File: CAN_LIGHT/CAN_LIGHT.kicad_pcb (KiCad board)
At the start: 2 copper layers, 135.5 x 115.4 mm, 180 parts, among them J1 Conn_ARM_SWD_TagConnect_TC2030, J2 436500428, J3 430450428, U1 MSPM0C1103SDDFR

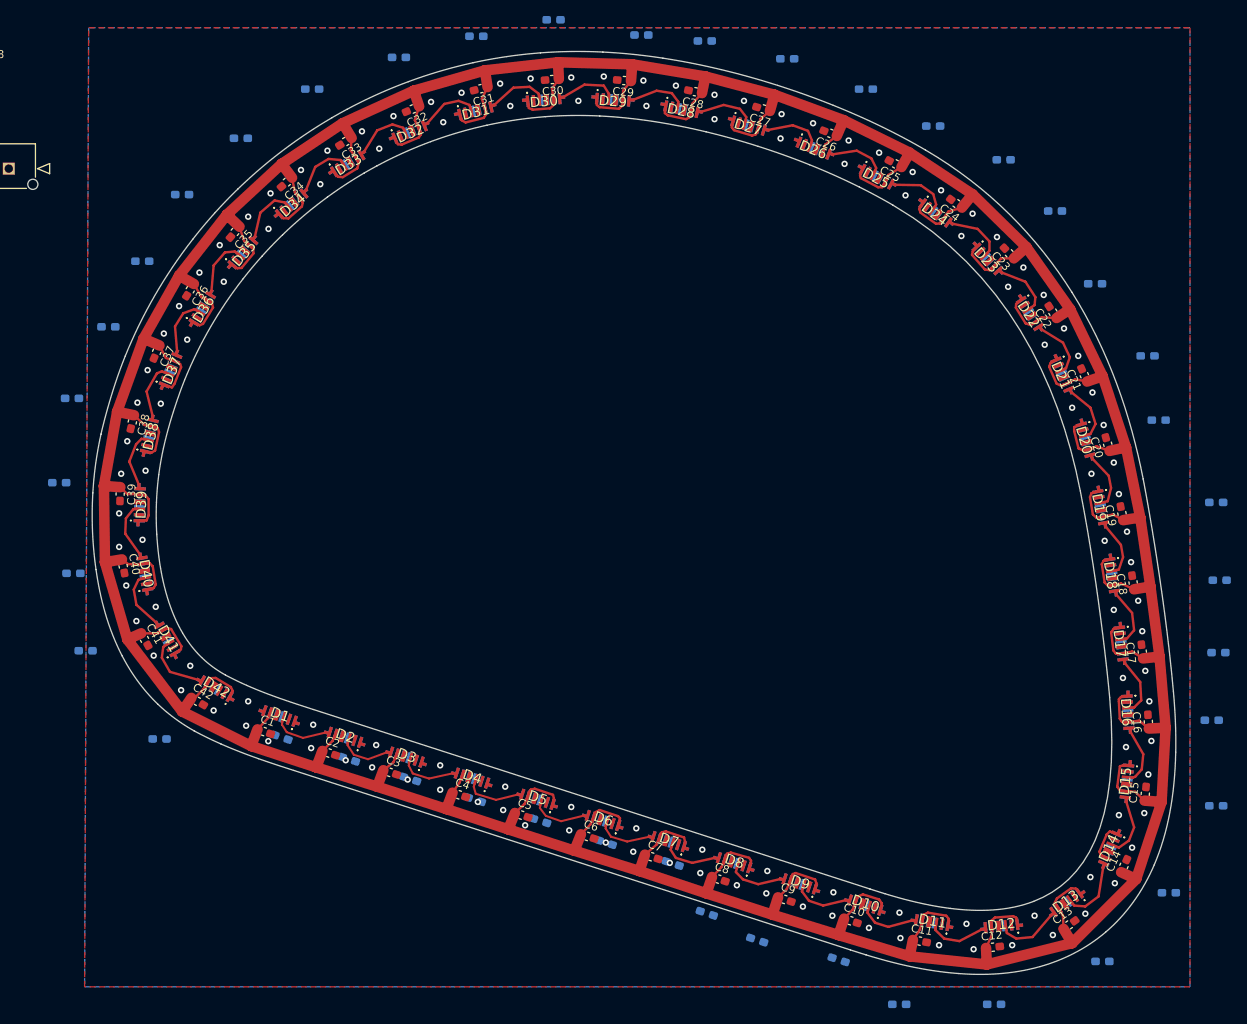
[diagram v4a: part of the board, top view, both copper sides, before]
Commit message: Roughly place caps; output updated PCB STEP file
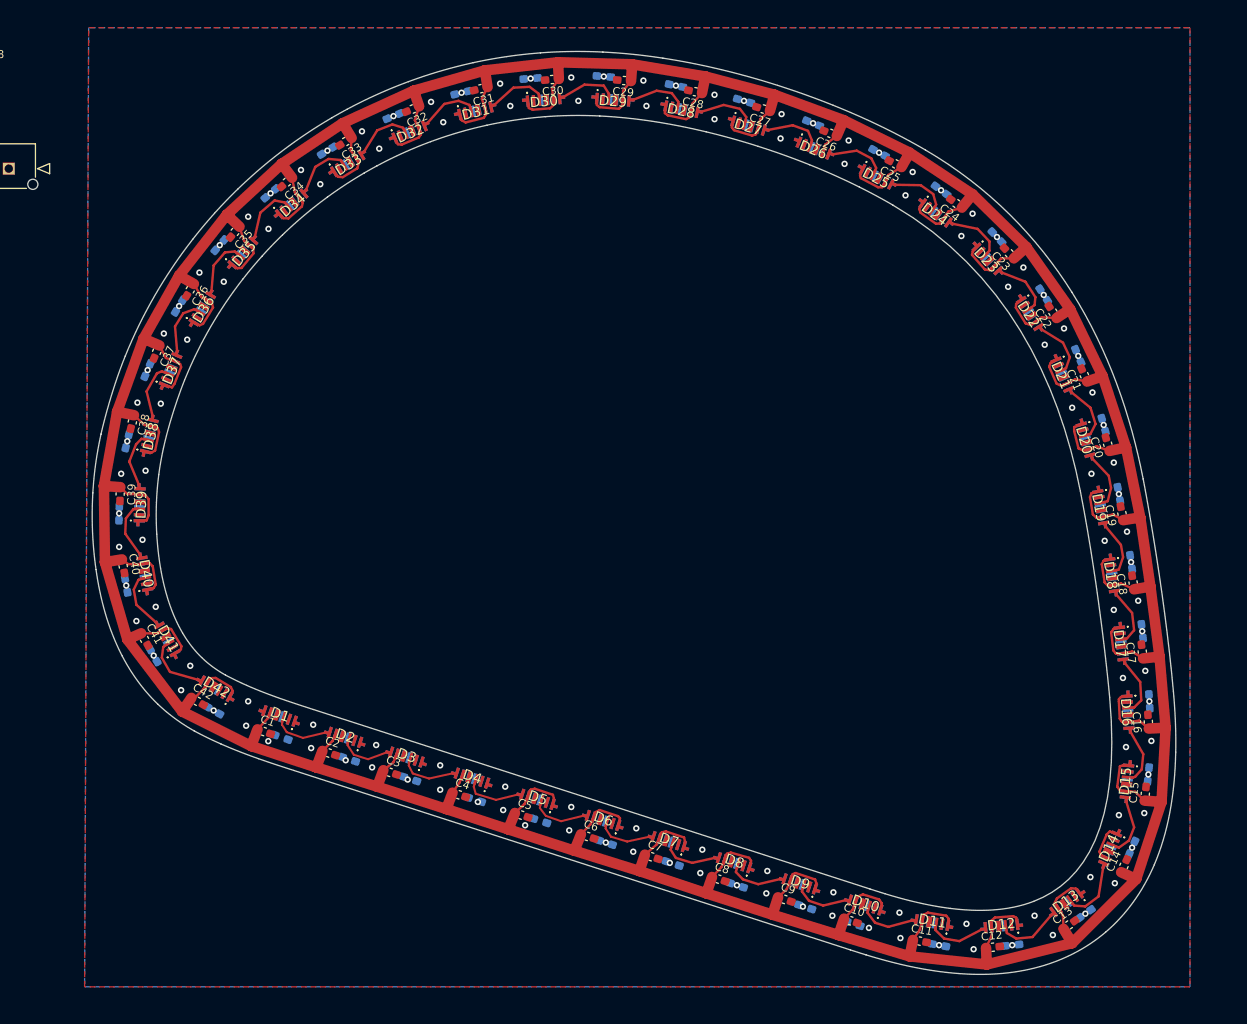
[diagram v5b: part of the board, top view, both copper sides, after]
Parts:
- moved C64 12.2 mm to (194.3, 83.1), turned to -79.5 degrees
- moved C63 11.3 mm to (195.8, 91.6), turned to -81.5 degrees
- moved C62 9.89 mm to (197.2, 100.2), turned to -83.5 degrees
- moved C60 9.34 mm to (198.0, 118.1), turned to -96 degrees
- moved C56 8.91 mm to (171.8, 139.4), turned to 170 degrees
- moved C83 8.74 mm to (70.4, 76.5), turned to 76.25 degrees
- moved C69 8.70 mm to (172.1, 45.1), turned to -36.5 degrees
- moved C66 8.66 mm to (189.2, 65.8), turned to -66.5 degrees
- moved C86 8.53 mm to (73.7, 103.3), turned to 119.25 degrees
- moved C84 8.42 mm to (69.3, 85.5), turned to 88.4 degrees
- moved C61 8.15 mm to (198.1, 109.0), turned to -86.5 degrees
- moved C68 7.96 mm to (179.1, 50.9), turned to -47 degrees
- moved C78 7.93 mm to (95.4, 40.1), turned to 31.5 degrees
- moved C75 7.88 mm to (120.8, 31.1), turned to 4.5 degrees
- moved C80 7.88 mm to (81.9, 51.9), turned to 49.25 degrees
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
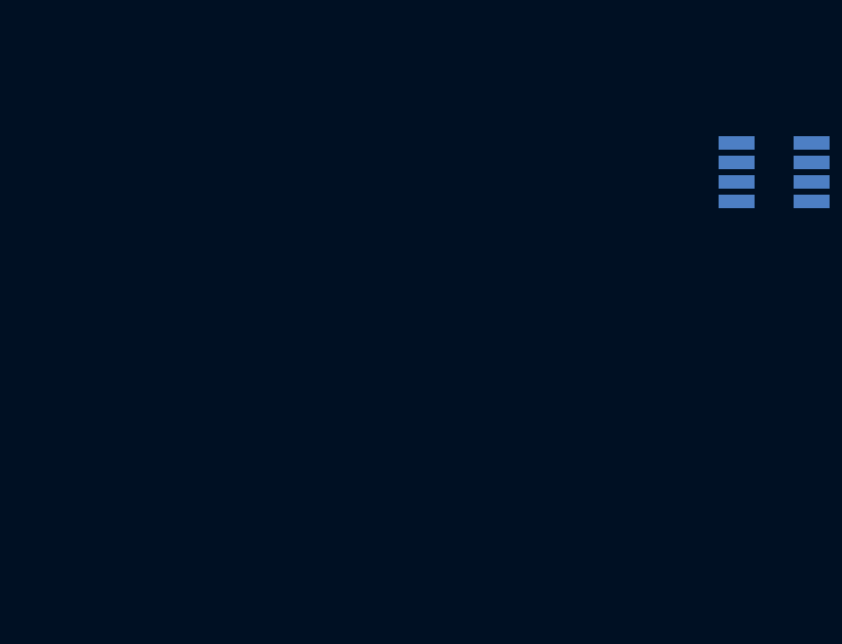
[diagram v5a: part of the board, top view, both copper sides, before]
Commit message: Select new MCU with CAN controller peripheral included
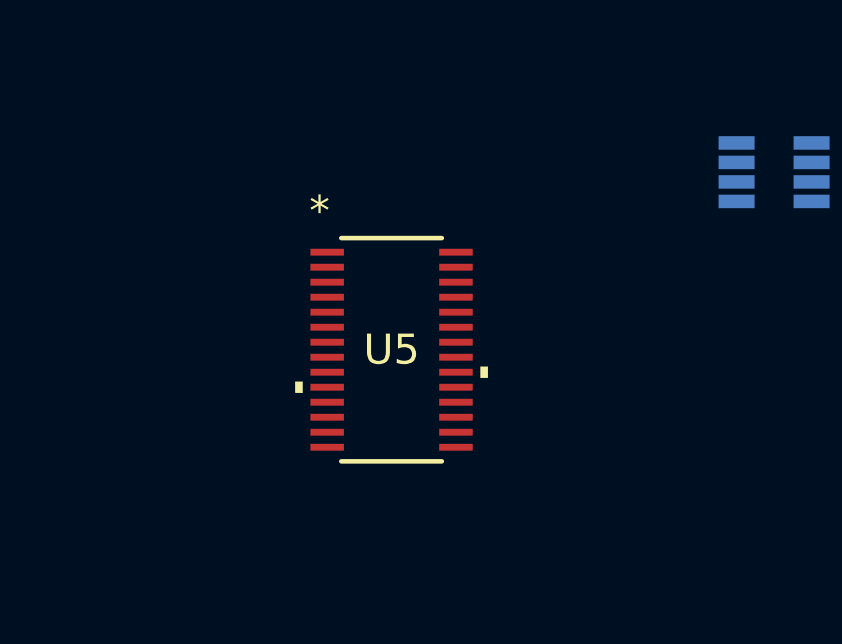
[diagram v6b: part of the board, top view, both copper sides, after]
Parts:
- added U5: XMSM0G3507SDGS28R, MSPM0G3507SDGS28R:VSSOP28_DGS_TEX-L, F.Cu at (35.1, 121.7)

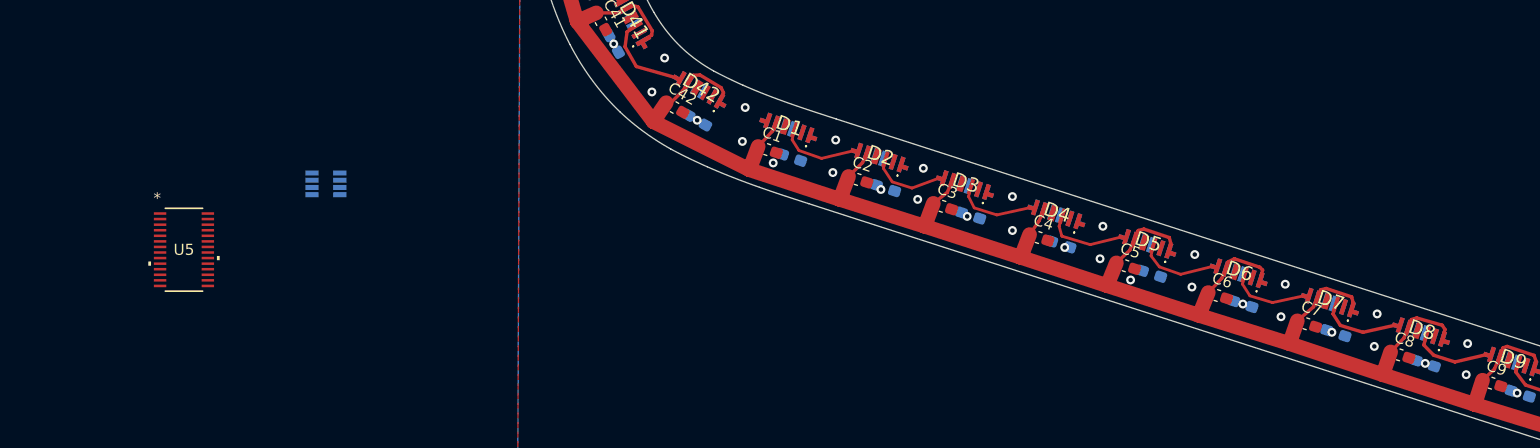
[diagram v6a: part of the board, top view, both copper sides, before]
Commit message: Update LED routing
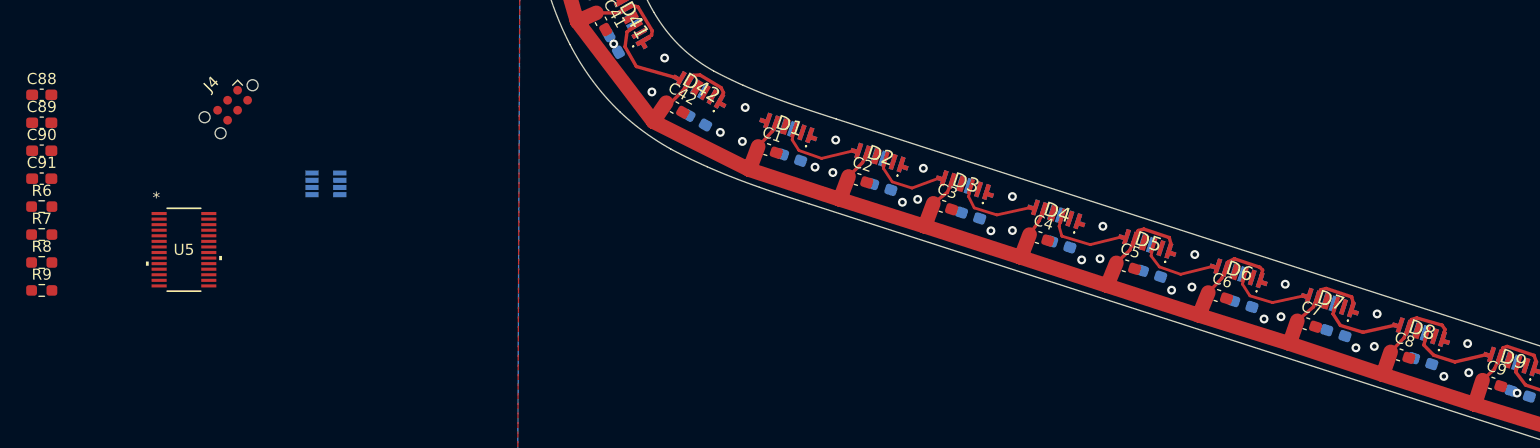
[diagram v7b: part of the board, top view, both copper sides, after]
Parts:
- added C88: 10nF, Capacitor_SMD:C_0603_1608Metric_Pad1.08x0.95mm_HandSolder, F.Cu at (22.3, 107.8)
- added C89: 10uF, Capacitor_SMD:C_0603_1608Metric_Pad1.08x0.95mm_HandSolder, F.Cu at (22.3, 110.3)
- added C90: 0.1uF, Capacitor_SMD:C_0603_1608Metric_Pad1.08x0.95mm_HandSolder, F.Cu at (22.3, 112.8)
- added C91: .47uF, Capacitor_SMD:C_0603_1608Metric_Pad1.08x0.95mm_HandSolder, F.Cu at (22.3, 115.4)
- added J4: Conn_ARM_SWD_TagConnect_TC2030-NL, Connector:Tag-Connect_TC2030-IDC-NL_2x03_P1.27mm_Vertical, F.Cu at (39.4, 108.8)
- added R6: 47K, Resistor_SMD:R_0603_1608Metric_Pad0.98x0.95mm_HandSolder, F.Cu at (22.3, 117.9)
- added R7: 100K, Resistor_SMD:R_0603_1608Metric_Pad0.98x0.95mm_HandSolder, F.Cu at (22.3, 120.4)
- added R8: 2.2K, Resistor_SMD:R_0603_1608Metric_Pad0.98x0.95mm_HandSolder, F.Cu at (22.3, 122.9)
- added R9: 2.2K, Resistor_SMD:R_0603_1608Metric_Pad0.98x0.95mm_HandSolder, F.Cu at (22.3, 125.4)
- U5: footprint MSPM0G3507SDGS28R:VSSOP28_DGS_TEX-L -> MSPM0G3507SDGS28R:VSSOP28_DGS_TEX
- moved C47 0.35 mm to (97.7, 116.1)
- moved C53 0.31 mm to (146.3, 131.7)
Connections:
- U5 pad 22: unconnected-(U5-PA19/SWDIO-Pad22) -> Net-(J4-SWDIO)
- U5 pad 23: unconnected-(U5-PA20/SWCLK-Pad23) -> Net-(J4-SWCLK)
- U5 pad 3: unconnected-(U5-VCORE-Pad3) -> Net-(U5-VCORE)
- U5 pad 4: unconnected-(U5-PA0-Pad4) -> Net-(U5-PA0)
- U5 pad 5: unconnected-(U5-PA1-Pad5) -> Net-(U5-PA1)
- U5 pad 6: unconnected-(U5-NRST-Pad6) -> Net-(J4-~{RESET})
- U5 pad 7: unconnected-(U5-VDD-Pad7) -> +3.3V
- U5 pad 8: unconnected-(U5-VSS-Pad8) -> GND
- U5 pad 9: unconnected-(U5-PA2_/_ROSC-Pad9) -> Net-(U5-PA2_/_ROSC)
